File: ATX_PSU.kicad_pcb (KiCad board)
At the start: 4 copper layers, 100 x 100 mm, 179 parts, among them J200 09031967921, J400 15246040, J401 Conn_01x06_Pin, J402 ATX-24, J800 USB_C_Receptacle_USB2.0_16P, Q404 AO3400A, Q409 AO3400A, Q410 HSBA8119, Q415 MMBT5551, Q416 AO3400A, Q417 HSBA8119, Q700 MMST3904, SW401 SW_SPDT, U100 W25Q128, U302 CH334P, U400 INA219AIDCNR, U401 TPD2E2U06DCK, U402 TPD2E2U06DCK, U405 STM32H562VGTx, U407 INA219AIDCNR, U408 INA219AIDCNR, U500 TJA1044GTK_3Z, U600 TJA1044GTK_3Z, U700 STM32F103CBTx, U801 FSUSB42UMX, X300 Q13FC1350000400, Y400 ASE-xxxMHz, Y700 8 MHz, Y900 12Mhz

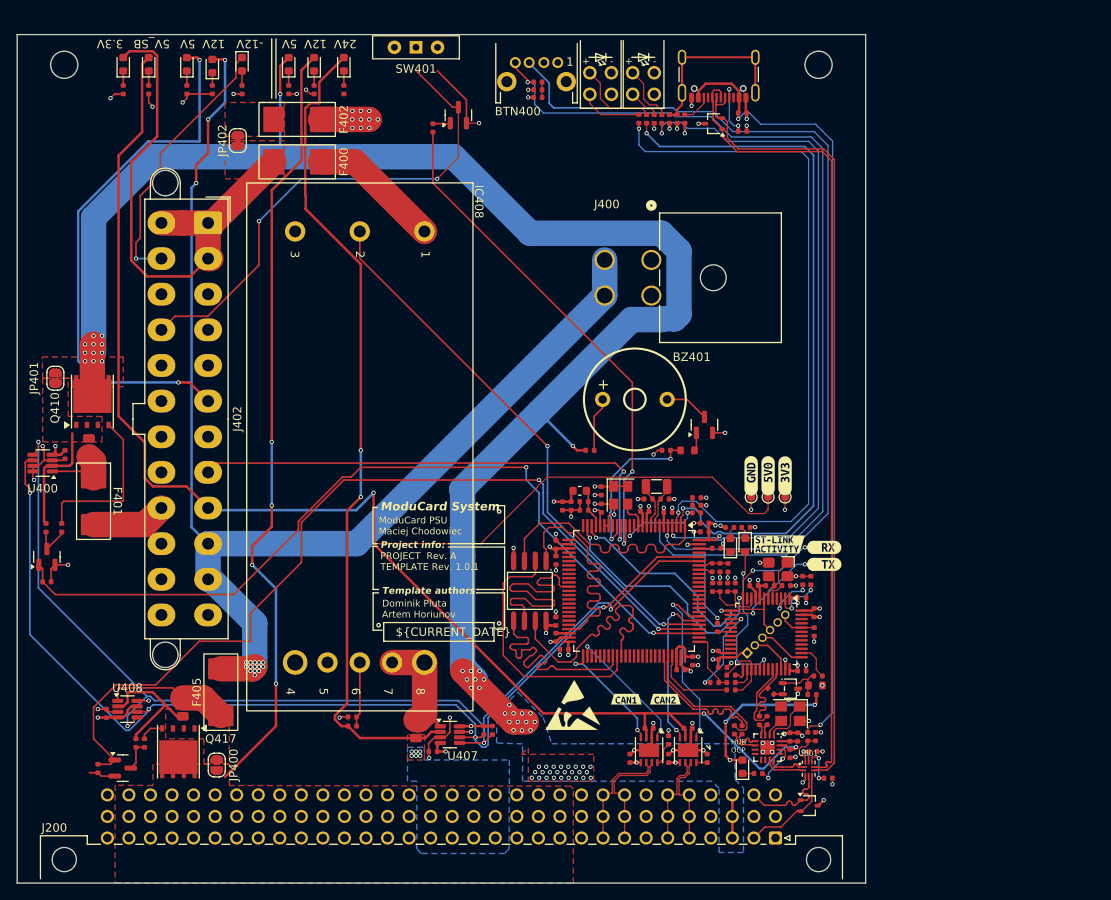
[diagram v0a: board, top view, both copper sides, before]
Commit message: layout rework
mostly done, PCBA to do
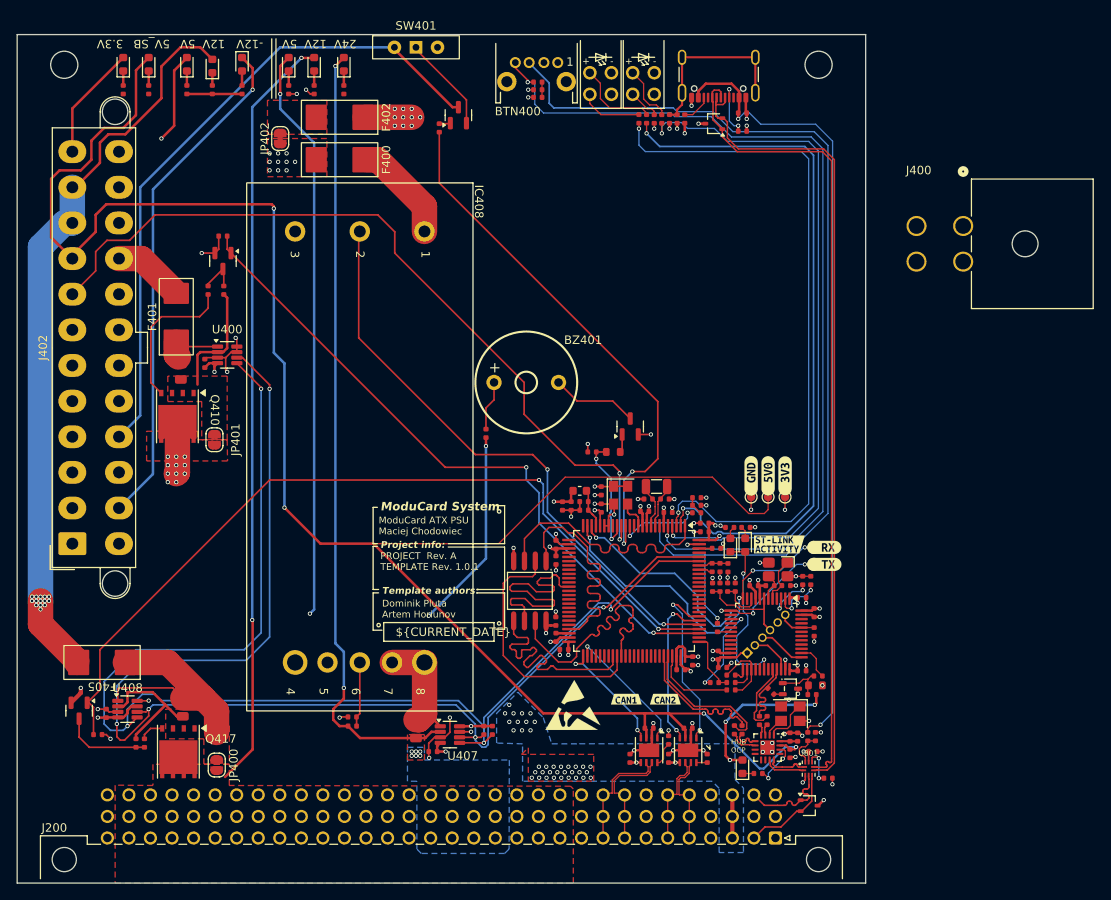
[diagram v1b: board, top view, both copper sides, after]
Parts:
- moved R456 45.7 mm to (63.6, 75.0), turned to 180 degrees
- moved J402 41.0 mm to (45.9, 111.3), turned to 90 degrees
- moved Q409 40.6 mm to (63.6, 78.0), turned to -90 degrees
- moved J400 37.0 mm to (150.9, 73.8)
- moved R457 35.0 mm to (63.7, 81.4), turned to 90 degrees
- moved R458 32.9 mm to (61.9, 81.4), turned to -90 degrees
- moved U400 25.2 mm to (64.1, 89.0), turned to 0 degrees
- moved F401 23.8 mm to (58.1, 84.5), turned to 90 degrees
- moved JP401 20.1 mm to (62.6, 99.0), turned to -90 degrees
- moved C409 19.7 mm to (61.5, 90.0), turned to 90 degrees
- moved F405 14.4 mm to (49.4, 125.3), turned to 180 degrees
- moved R455 13.9 mm to (58.7, 91.0), turned to -90 degrees
- moved BZ401 13.0 mm to (99.4, 92.3)
- moved R445 12.4 mm to (94.6, 98.3), turned to 90 degrees
- moved Q410 10.2 mm to (58.3, 96.3), turned to -90 degrees
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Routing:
- net /ATX connector/+5V_ATX: track 175.4 -> 107.8 mm, vias 2 -> 1
- net /ATX connector/+12V_ATX: track 145.2 -> 87.6 mm, vias 17 -> 14
- net +5V: track 216.7 -> 180.3 mm, vias 61 -> 55
- net /ATX connector/PWR_OK_ATX: track 59.8 -> 95.6 mm
- net /ATX connector/-12V_ATX: track 31.9 -> 60.1 mm
- net /MCU/I2C1.SDA: track 125.3 -> 151.1 mm, vias 4 -> 5
- net /MCU/I2C1.SCL: track 126.5 -> 152.2 mm
- net +5V_SB: track 211.9 -> 232.7 mm, vias 3 -> 4
- net /MCU/ON-OFF0: track 98.1 -> 78.9 mm
- net /ATX connector/PS_ON#_ATX: track 59.2 -> 77.8 mm, vias 2 -> 0
- net Net-(U408-IN+): track 14.9 -> 27.6 mm
- net /ATX connector/+3.3V_ATX: track 106.9 -> 116.4 mm, vias 0 -> 10
- net Net-(Q416-D): track 3.71 -> 10.4 mm
- net /MCU/ON-OFF1: track 106.0 -> 99.4 mm
- net /MCU/Buzzer: track 19.3 -> 14.1 mm
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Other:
- board text added: "ModuCard ATX PSU ${COMMENT2}"
- board text removed: "ModuCard PSU ${COMMENT2}"

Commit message: add 2x6pin PCIe molex + PCBA to check
should work now
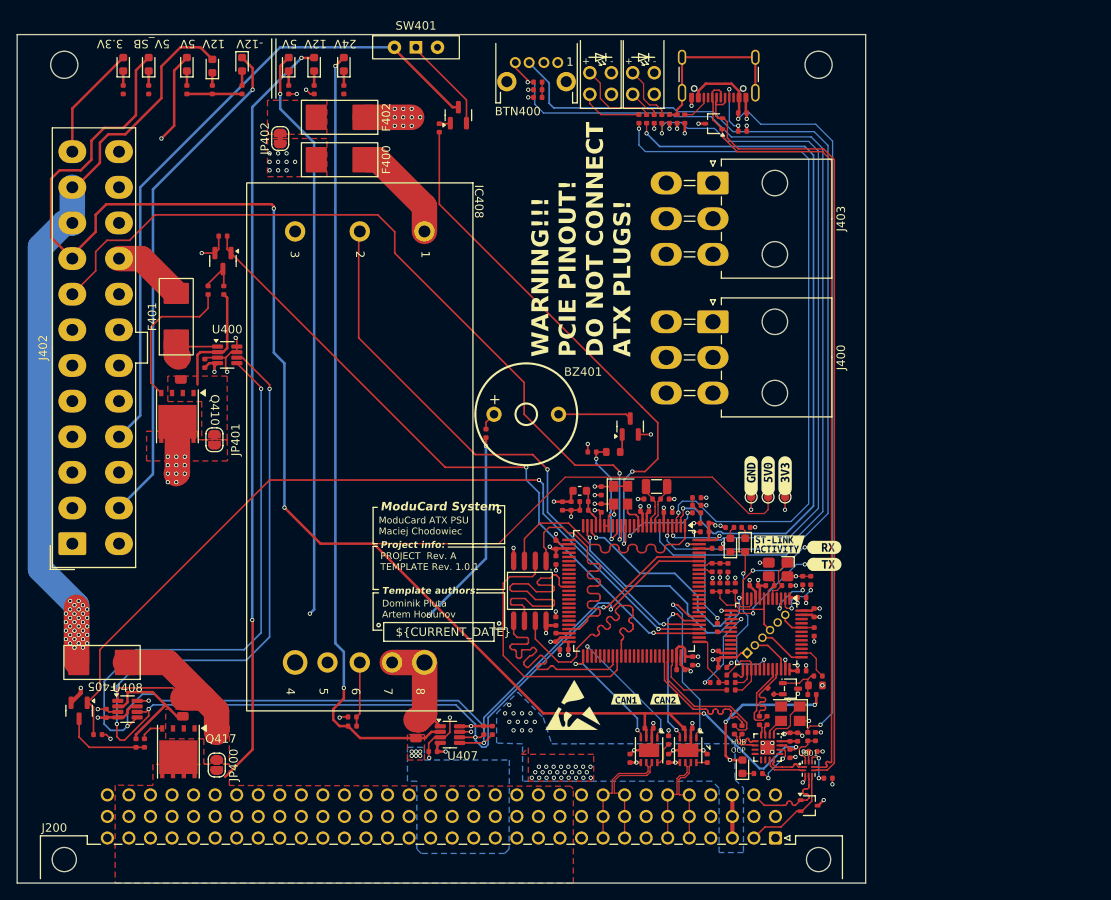
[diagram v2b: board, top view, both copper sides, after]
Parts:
- added J403: Conn_02x03_Top_Bottom, Connector_Molex:Molex_Mini-Fit_Jr_5569-06A2_2x03_P4.20mm_Horizontal, F.Cu at (121.4, 68.8)
- J400: value 15246040 -> Conn_02x03_Top_Bottom; footprint footprints:CONN_SDA-42404_04_MOL -> Connector_Molex:Molex_Mini-Fit_Jr_5569-06A2_2x03_P4.20mm_Horizontal
- J402: footprint Connector_Molex:Molex_Mini-Fit_Jr_5566-24A2_2x12_P4.20mm_Vertical -> Connector_Molex:Molex_Mini-Fit_Jr_5566-24A_2x12_P4.20mm_Vertical
- moved J400 31.6 mm to (121.4, 85.1), turned to -90 degrees
- moved BZ401 3.75 mm to (99.4, 96.0)
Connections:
- J400 pad 1: GND -> /ATX connector/+12V_ATX
- J400 pad 2: GND -> /ATX connector/+12V_ATX
- J400 pad 4: /ATX connector/+12V_ATX -> GND
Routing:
- net /ATX connector/+12V_ATX: track 87.6 -> 211.9 mm, vias 14 -> 33
- net /ATX connector/+5V_ATX: track 107.8 -> 103.1 mm
- net Net-(BZ401-+): track 5.89 -> 2.14 mm
- net Net-(BZ401--): track 10.2 -> 8.66 mm
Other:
- board text added: "WARNING!!! PCIE PINOUT! DO NOT CONNECT ATX PLUGS!"
